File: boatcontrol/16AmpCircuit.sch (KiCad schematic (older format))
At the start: 5 parts, among them K6601 G5RL-K1A-E-DC12, Q6601 T9-818 16A, SW6601 ESB30, SW6602 ESB30

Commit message: More cleanup
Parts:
- D6601: value WP115VGYW -> 20mA R/G CA; Manufacturer (none) -> Kingbright; Model (none) -> WP59EGW/CA

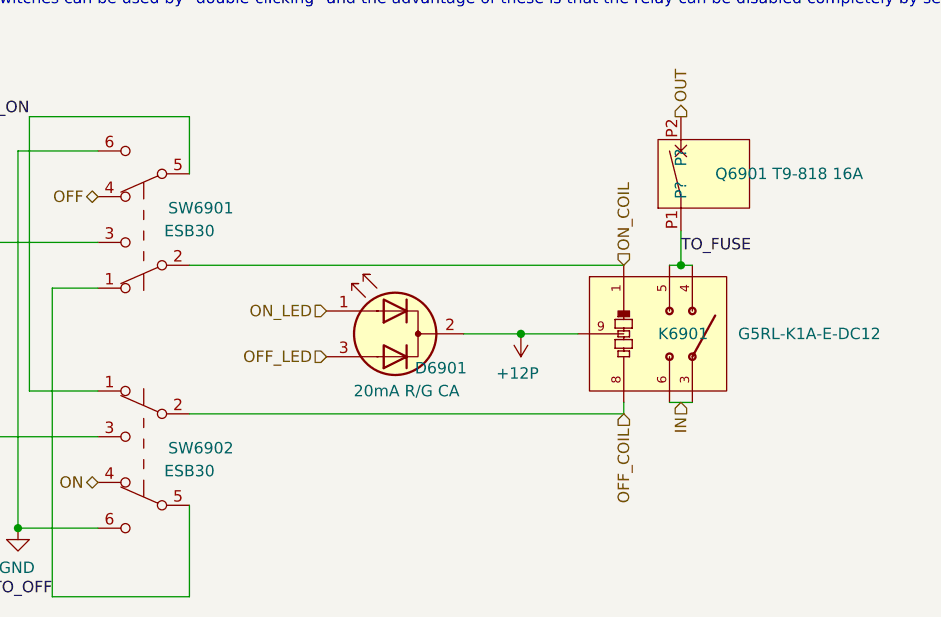
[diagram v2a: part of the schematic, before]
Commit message: Add Node-RED flows
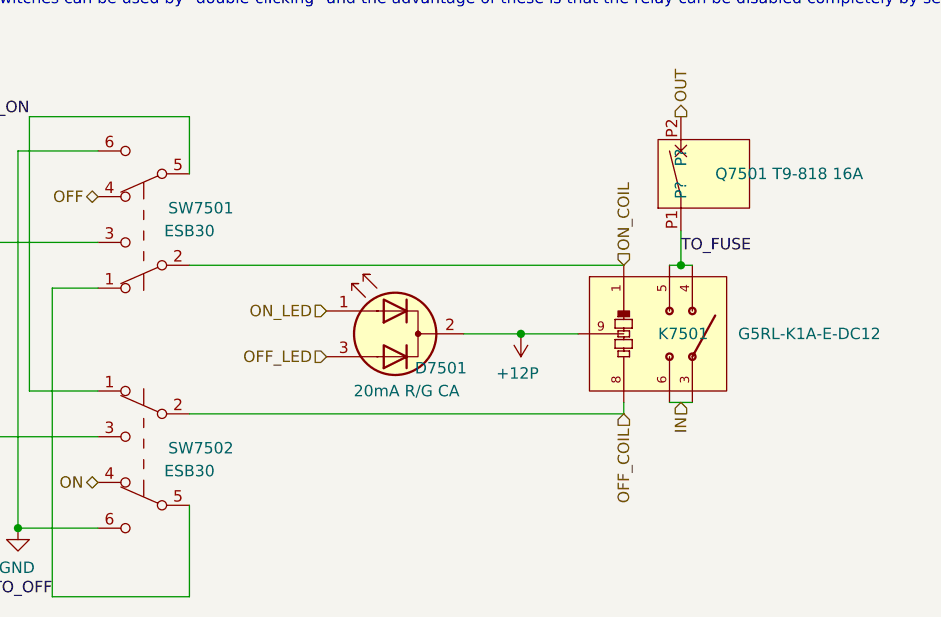
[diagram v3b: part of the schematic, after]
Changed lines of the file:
@@
 AR Path="/D1BB8DB4/5F75E923/604748F7/E14E2028" Ref="K7501"  Part="1"
 AR Path="/D1BB8DB4/5F75E923/604748FF/E14E2028" Ref="K7801"  Part="1"
-F 0 "K6901" H 6550 4200 50  0000 L CNN
+F 0 "K7501" H 6550 4200 50  0000 L CNN
 F 1 "G5RL-K1A-E-DC12" H 6900 4200 50  0000 L CNN
 F 2 "RELAY_G5RL-K1A-E-DC12" H 6900 4350 50  0001 L BNN
@@
 AR Path="/D1BB8DB4/5F75E923/604748F7/E14E2029" Ref="Q7501"  Part="1"
 AR Path="/D1BB8DB4/5F75E923/604748FF/E14E2029" Ref="Q7801"  Part="1"
-F 0 "Q6901" V 6450 3150 50  0000 R CNN
+F 0 "Q7501" V 6450 3150 50  0000 R CNN
 F 1 "T9-818 16A" V 6450 2900 50  0000 R CNN
 F 2 "BoatControl:Schurter_Circuit_Breaker" H 6450 3500 50  0001 C CNN
@@
 AR Path="/D1BB8DB4/5F75E923/604748F7/E14E202A" Ref="SW7501"  Part="1"
 AR Path="/D1BB8DB4/5F75E923/604748FF/E14E202A" Ref="SW7801"  Part="1"
-F 0 "SW6901" H 4050 3650 50  0000 C CNN
+F 0 "SW7501" H 4050 3650 50  0000 C CNN
 F 1 " ESB30" H 4100 3750 50  0000 C CNN
 F 2 "BoatControl:SW_PUSH_ESB30_DPDT" H 4300 3900 50  0001 C CNN
@@
 AR Path="/D1BB8DB4/5F75E923/604748F7/62834852" Ref="SW7502"  Part="1"
 AR Path="/D1BB8DB4/5F75E923/604748FF/62834852" Ref="SW7802"  Part="1"
-F 0 "SW6902" H 4050 4800 50  0000 C CNN
+F 0 "SW7502" H 4050 4800 50  0000 C CNN
 F 1 " ESB30" H 4100 4700 50  0000 C CNN
 F 2 "BoatControl:SW_PUSH_ESB30_DPDT" H 4300 4950 50  0001 C CNN
@@
 AR Path="/D1BB8DB4/5F75E923/604748FF/5FFCB425" Ref="D7801"  Part="1"
 AR Path="/D1BB8DB4/5F75E923/604748F7/5FFCB425" Ref="D7501"  Part="1"
-F 0 "D6901" H 5200 4050 50  0000 C CNN
+F 0 "D7501" H 5200 4050 50  0000 C CNN
 F 1 "20mA R/G CA" H 5350 3950 50  0000 C CNN
 F 2 "LED_THT:LED_D5.0mm-3" H 5400 4200 50  0001 C CNN

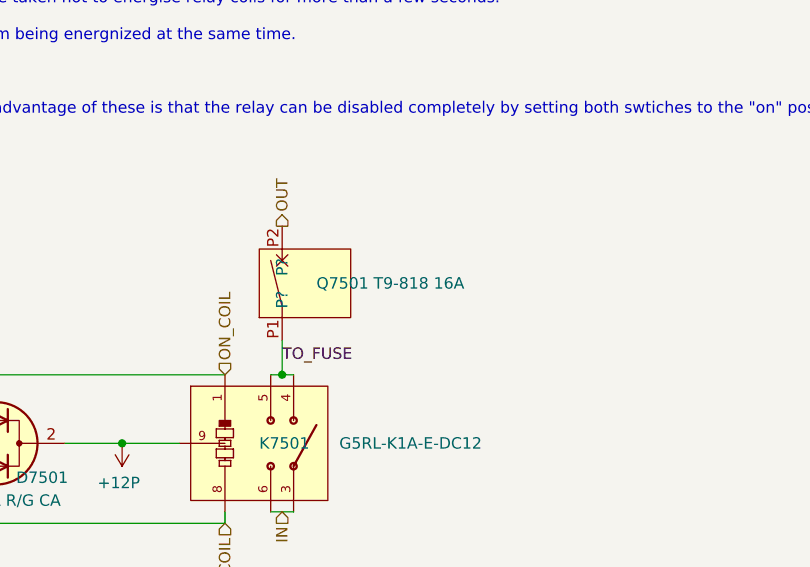
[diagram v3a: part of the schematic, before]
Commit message: Fix SB footprint and symbol
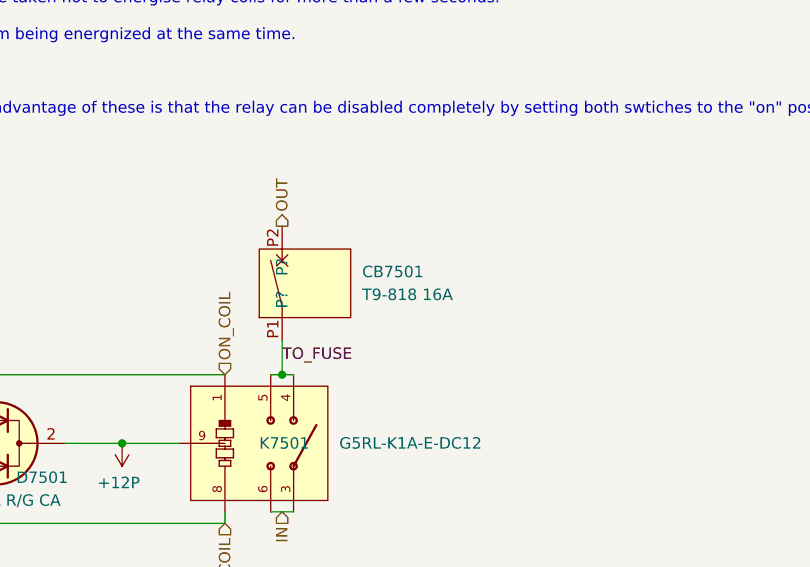
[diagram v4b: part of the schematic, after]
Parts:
- renumbered Q6601 to CB6601
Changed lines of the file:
@@
 $Descr A4 11693 8268
 encoding utf-8
-Sheet 77 97
+Sheet 75 97
 Title "Boat Control Hat"
 Date "2020-07-09"
@@
 AR Path="/D16552B4/5FA17F86/81A9CCB4/E14E2029" Ref="Q?"  Part="1"
 AR Path="/D16552B4/5FA17F86/81A9CCAC/E14E2029" Ref="Q?"  Part="1"
-AR Path="/D1BB8DB4/5F76AF55/604748F7/E14E2029" Ref="Q6601"  Part="1"
-AR Path="/D1BB8DB4/5F76AF55/604748FF/E14E2029" Ref="Q6901"  Part="1"
-AR Path="/D1BB8DB4/5F75E923/604748F7/E14E2029" Ref="Q7501"  Part="1"
-AR Path="/D1BB8DB4/5F75E923/604748FF/E14E2029" Ref="Q7801"  Part="1"
-F 0 "Q7501" V 6450 3150 50  0000 R CNN
-F 1 "T9-818 16A" V 6450 2900 50  0000 R CNN
+AR Path="/D1BB8DB4/5F76AF55/604748F7/E14E2029" Ref="CB6601"  Part="1"
+AR Path="/D1BB8DB4/5F76AF55/604748FF/E14E2029" Ref="CB6901"  Part="1"
+AR Path="/D1BB8DB4/5F75E923/604748F7/E14E2029" Ref="CB7501"  Part="1"
+AR Path="/D1BB8DB4/5F75E923/604748FF/E14E2029" Ref="CB7801"  Part="1"
+F 0 "CB7501" V 6500 2950 50  0000 R CNN
+F 1 "T9-818 16A" V 6400 2950 50  0000 R CNN
 F 2 "BoatControl:Schurter_Circuit_Breaker" H 6450 3500 50  0001 C CNN
 F 3 "https://eu.mouser.com/datasheet/2/358/typ_T9-818-1276014.pdf" H 6450 3500 50  0001 C CNN

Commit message: Cleanup
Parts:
- D6601: symbol Device:LED_Dual_ACA -> boatcontrol-rescue:LED_Dual_ACA-Device
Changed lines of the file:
@@
 ON_TO_OFF
 $Comp
-L Device:LED_Dual_ACA D?
+L boatcontrol-rescue:LED_Dual_ACA-Device D?
 U 1 1 5FFCB425
 P 5400 4200

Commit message: mwire
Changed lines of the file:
@@
 $Descr A4 11693 8268
 encoding utf-8
-Sheet 75 97
+Sheet 55 97
 Title "Boat Control Hat"
 Date "2020-07-09"
@@
 AR Path="/D1BB8DB4/5F75E923/604748F7/E14E2028" Ref="K7501"  Part="1"
 AR Path="/D1BB8DB4/5F75E923/604748FF/E14E2028" Ref="K7801"  Part="1"
-F 0 "K7501" H 6550 4200 50  0000 L CNN
+F 0 "K6601" H 6550 4200 50  0000 L CNN
 F 1 "G5RL-K1A-E-DC12" H 6900 4200 50  0000 L CNN
 F 2 "RELAY_G5RL-K1A-E-DC12" H 6900 4350 50  0001 L BNN
@@
 AR Path="/D1BB8DB4/5F75E923/604748F7/E14E2029" Ref="CB7501"  Part="1"
 AR Path="/D1BB8DB4/5F75E923/604748FF/E14E2029" Ref="CB7801"  Part="1"
-F 0 "CB7501" V 6500 2950 50  0000 R CNN
+F 0 "CB6601" V 6500 2950 50  0000 R CNN
 F 1 "T9-818 16A" V 6400 2950 50  0000 R CNN
 F 2 "BoatControl:Schurter_Circuit_Breaker" H 6450 3500 50  0001 C CNN
@@
 AR Path="/D1BB8DB4/5F75E923/604748F7/E14E202A" Ref="SW7501"  Part="1"
 AR Path="/D1BB8DB4/5F75E923/604748FF/E14E202A" Ref="SW7801"  Part="1"
-F 0 "SW7501" H 4050 3650 50  0000 C CNN
+F 0 "SW6601" H 4050 3650 50  0000 C CNN
 F 1 " ESB30" H 4100 3750 50  0000 C CNN
 F 2 "BoatControl:SW_PUSH_ESB30_DPDT" H 4300 3900 50  0001 C CNN
@@
 AR Path="/D1BB8DB4/5F75E923/604748F7/62834852" Ref="SW7502"  Part="1"
 AR Path="/D1BB8DB4/5F75E923/604748FF/62834852" Ref="SW7802"  Part="1"
-F 0 "SW7502" H 4050 4800 50  0000 C CNN
+F 0 "SW6602" H 4050 4800 50  0000 C CNN
 F 1 " ESB30" H 4100 4700 50  0000 C CNN
 F 2 "BoatControl:SW_PUSH_ESB30_DPDT" H 4300 4950 50  0001 C CNN
@@
 AR Path="/D1BB8DB4/5F75E923/604748FF/5FFCB425" Ref="D7801"  Part="1"
 AR Path="/D1BB8DB4/5F75E923/604748F7/5FFCB425" Ref="D7501"  Part="1"
-F 0 "D7501" H 5200 4050 50  0000 C CNN
+F 0 "D6601" H 5200 4050 50  0000 C CNN
 F 1 "20mA R/G CA" H 5350 3950 50  0000 C CNN
 F 2 "LED_THT:LED_D5.0mm-3" H 5400 4200 50  0001 C CNN

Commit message: Move centre right
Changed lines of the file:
@@
 AR Path="/D1BB8DB4/5F75E923/604748F7/E14E2028" Ref="K7501"  Part="1"
 AR Path="/D1BB8DB4/5F75E923/604748FF/E14E2028" Ref="K7801"  Part="1"
-F 0 "K6601" H 6550 4200 50  0000 L CNN
+F 0 "K7501" H 6550 4200 50  0000 L CNN
 F 1 "G5RL-K1A-E-DC12" H 6900 4200 50  0000 L CNN
 F 2 "RELAY_G5RL-K1A-E-DC12" H 6900 4350 50  0001 L BNN
@@
 AR Path="/D1BB8DB4/5F75E923/604748F7/E14E2029" Ref="CB7501"  Part="1"
 AR Path="/D1BB8DB4/5F75E923/604748FF/E14E2029" Ref="CB7801"  Part="1"
-F 0 "CB6601" V 6500 2950 50  0000 R CNN
+F 0 "CB7501" V 6500 2950 50  0000 R CNN
 F 1 "T9-818 16A" V 6400 2950 50  0000 R CNN
 F 2 "BoatControl:Schurter_Circuit_Breaker" H 6450 3500 50  0001 C CNN
@@
 AR Path="/D1BB8DB4/5F75E923/604748F7/E14E202A" Ref="SW7501"  Part="1"
 AR Path="/D1BB8DB4/5F75E923/604748FF/E14E202A" Ref="SW7801"  Part="1"
-F 0 "SW6601" H 4050 3650 50  0000 C CNN
+F 0 "SW7501" H 4050 3650 50  0000 C CNN
 F 1 " ESB30" H 4100 3750 50  0000 C CNN
 F 2 "BoatControl:SW_PUSH_ESB30_DPDT" H 4300 3900 50  0001 C CNN
@@
 AR Path="/D1BB8DB4/5F75E923/604748F7/62834852" Ref="SW7502"  Part="1"
 AR Path="/D1BB8DB4/5F75E923/604748FF/62834852" Ref="SW7802"  Part="1"
-F 0 "SW6602" H 4050 4800 50  0000 C CNN
+F 0 "SW7502" H 4050 4800 50  0000 C CNN
 F 1 " ESB30" H 4100 4700 50  0000 C CNN
 F 2 "BoatControl:SW_PUSH_ESB30_DPDT" H 4300 4950 50  0001 C CNN
@@
 AR Path="/D1BB8DB4/5F75E923/604748FF/5FFCB425" Ref="D7801"  Part="1"
 AR Path="/D1BB8DB4/5F75E923/604748F7/5FFCB425" Ref="D7501"  Part="1"
-F 0 "D6601" H 5200 4050 50  0000 C CNN
+F 0 "D7501" H 5200 4050 50  0000 C CNN
 F 1 "20mA R/G CA" H 5350 3950 50  0000 C CNN
 F 2 "LED_THT:LED_D5.0mm-3" H 5400 4200 50  0001 C CNN

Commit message: Fix rescued symbols
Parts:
- D6601: symbol boatcontrol-rescue:LED_Dual_ACA-Device -> Device:LED_Dual_AKA
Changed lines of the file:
@@
 ON_TO_OFF
 $Comp
-L boatcontrol-rescue:LED_Dual_ACA-Device D?
+L Device:LED_Dual_AKA D?
 U 1 1 5FFCB425
 P 5400 4200
